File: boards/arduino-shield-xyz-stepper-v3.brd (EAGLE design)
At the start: 73.7 x 55.5 mm, 10 parts, among them IC1 2967-MP6500, IC2 2967-MP6500, IC3 2967-MP6500, J4 ARDUINO_R3_SHIELD, J6 455-1750-1-ND

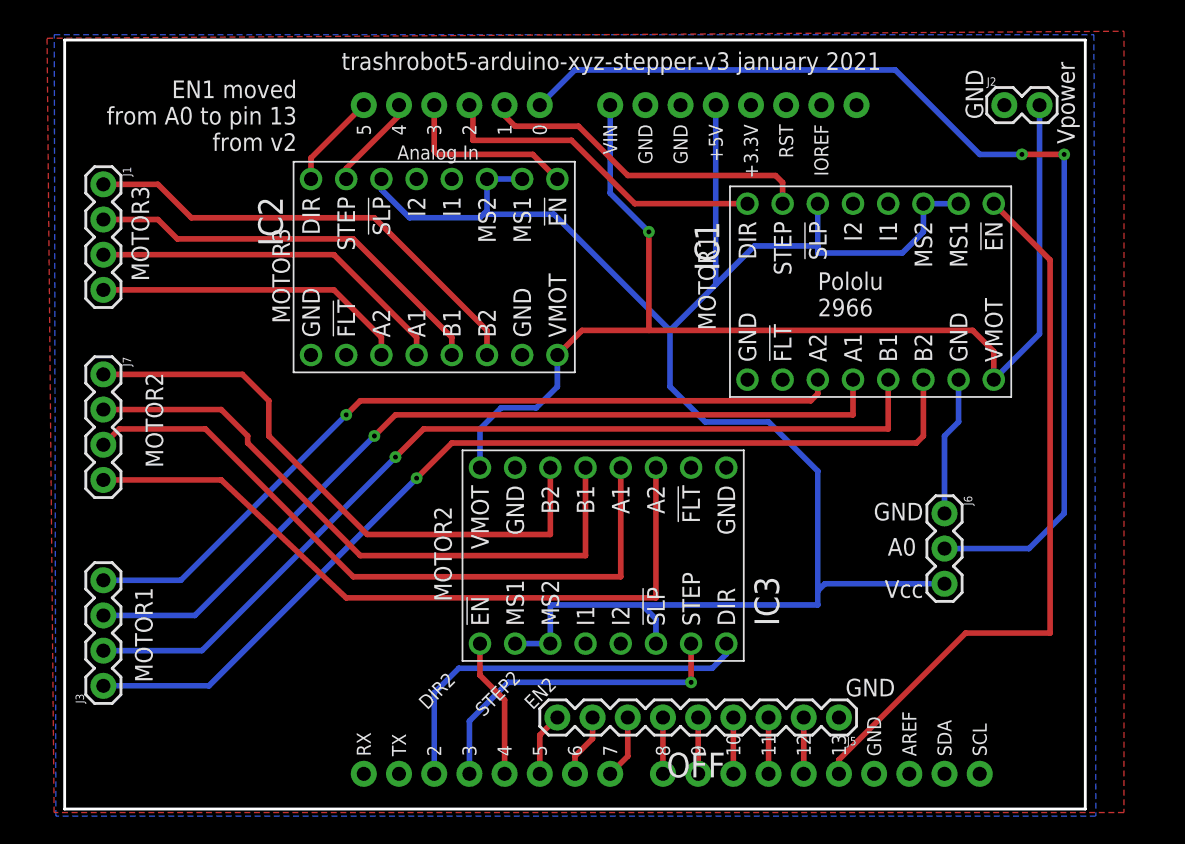
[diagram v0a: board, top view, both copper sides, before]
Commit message: better robot code, new board version
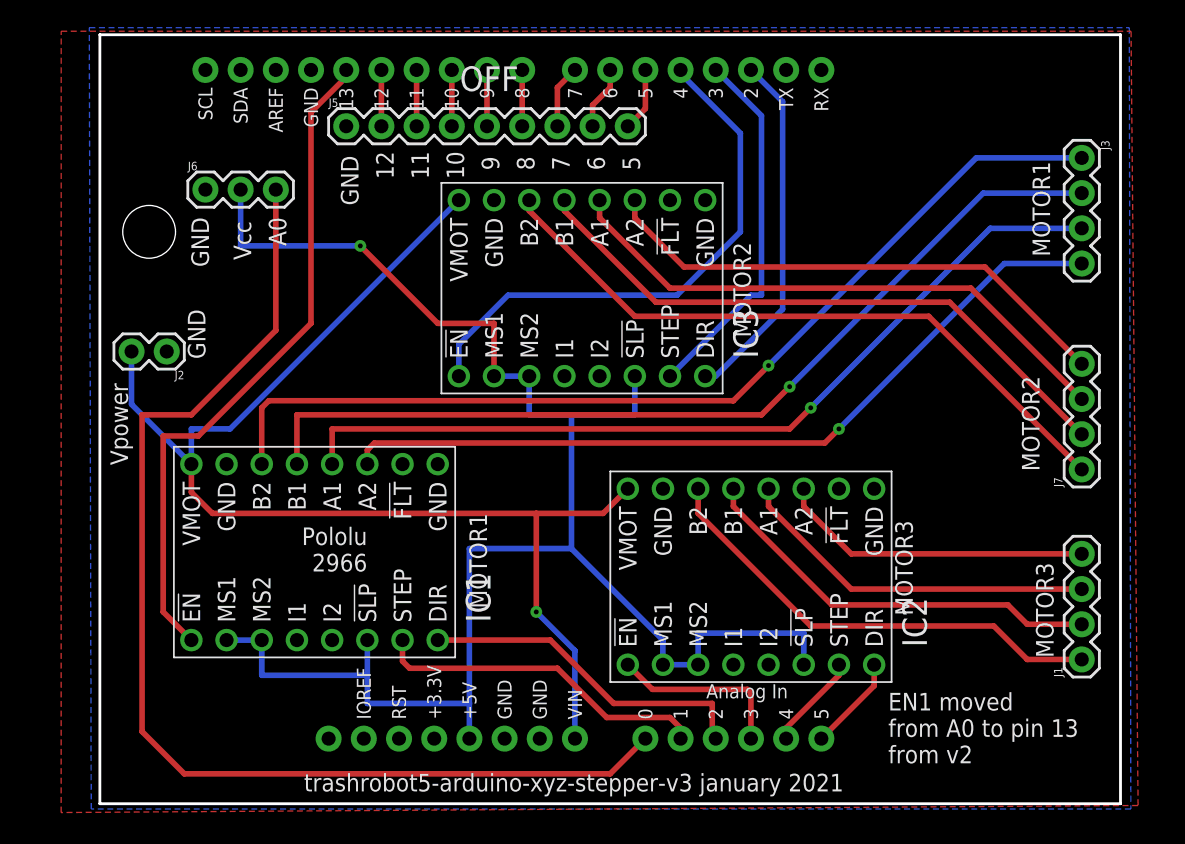
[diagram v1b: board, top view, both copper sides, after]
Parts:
- moved J4 94.5 mm to (0.00, 55.9), turned to 270 degrees
- moved J3 80.2 mm to (73.4, 47.0), turned to 270 degrees
- moved J1 78.5 mm to (73.4, 10.8), turned to 90 degrees
- moved J7 70.9 mm to (73.4, 24.5), turned to 90 degrees
- moved J2 63.0 mm to (7.37, 33.0), turned to 180 degrees
- moved J6 58.2 mm to (10.2, 44.7), turned to 0 degrees
- moved J5 55.5 mm to (20.3, 49.3), turned to 0 degrees
- moved IC1 44.3 mm to (18.0, 18.5), turned to 90 degrees
- moved IC2 32.0 mm to (49.5, 16.8), turned to 90 degrees
- moved IC3 19.4 mm to (37.3, 37.6)
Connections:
- removed net A0: J4.A0, J6.2
- new net N$15: J4.A0, J6.3
- net 5V: now also J6.2; no longer J6.3
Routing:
- net N$15: track 0.00 -> 83.8 mm
- net A0: track 77.0 -> 0.00 mm, vias 2 -> 0
- net EN2: track 10.1 -> 39.4 mm
- net N$14: track 52.7 -> 37.9 mm
- net 5V: track 137.8 -> 125.4 mm, vias 0 -> 1
- net GND: track 10.1 -> 0.00 mm
- net N$13: track 50.1 -> 41.5 mm
- net 12V: track 85.4 -> 90.9 mm
- net N$1: track 43.4 -> 48.4 mm
- net EN1: track 52.7 -> 48.9 mm
- net DIR2: track 28.8 -> 25.8 mm
- net STEP2: track 23.8 -> 26.6 mm, vias 1 -> 0
- net N$4: track 45.8 -> 44.8 mm
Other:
- board text added: "10"
- board text added: "11"
- board text added: "12"
- board text added: "5"
- board text added: "6"
- board text added: "7"
- board text added: "8"
- board text added: "9"
- board text removed: "DIR2"
- board text removed: "EN2"
- board text removed: "STEP2"
